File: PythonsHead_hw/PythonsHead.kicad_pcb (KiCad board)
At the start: 2 copper layers, 88.4 x 78.7 mm, 254 parts, among them Q1 IRLML9303, Q10 IRLML9303, Q11 IRLML9303, Q12 IRLML9303, Q13 IRLML6401, Q14 IRLML6244, Q15 IRLML6401, Q16 IRLML6244, Q17 IRLML6401, Q18 IRLML6244, Q19 IRLML6401, Q2 IRLML9303, Q20 IRLML6244, Q21 IRLML6401, Q22 IRLML6244, Q23 IRLML6401, Q24 IRLML6244, Q25 IRLML6401, Q26 IRLML6244, Q27 IRLML6401, Q28 IRLML6244, Q29 IRLML9303, Q3 IRLML9303, Q30 IRLML9303, Q31 IRLML9303, Q32 IRLML9303, Q33 IRLML6401, Q34 IRLML6244, Q35 IRLML6401, Q36 IRLML6244, Q37 IRLML6401, Q38 IRLML6244, Q39 IRLML6401, Q4 IRLML9303, Q40 IRLML6244, Q41 IRLML6401, Q42 IRLML6244, Q43 IRLML6401, Q44 IRLML6244, Q45 IRLML6401, Q46 IRLML6244, Q47 IRLML6401, Q48 IRLML6244, Q49 IRF8313, Q5 IRLML9303, Q6 IRLML9303, Q7 IRLML9303, Q8 IRLML9303, Q9 IRLML9303

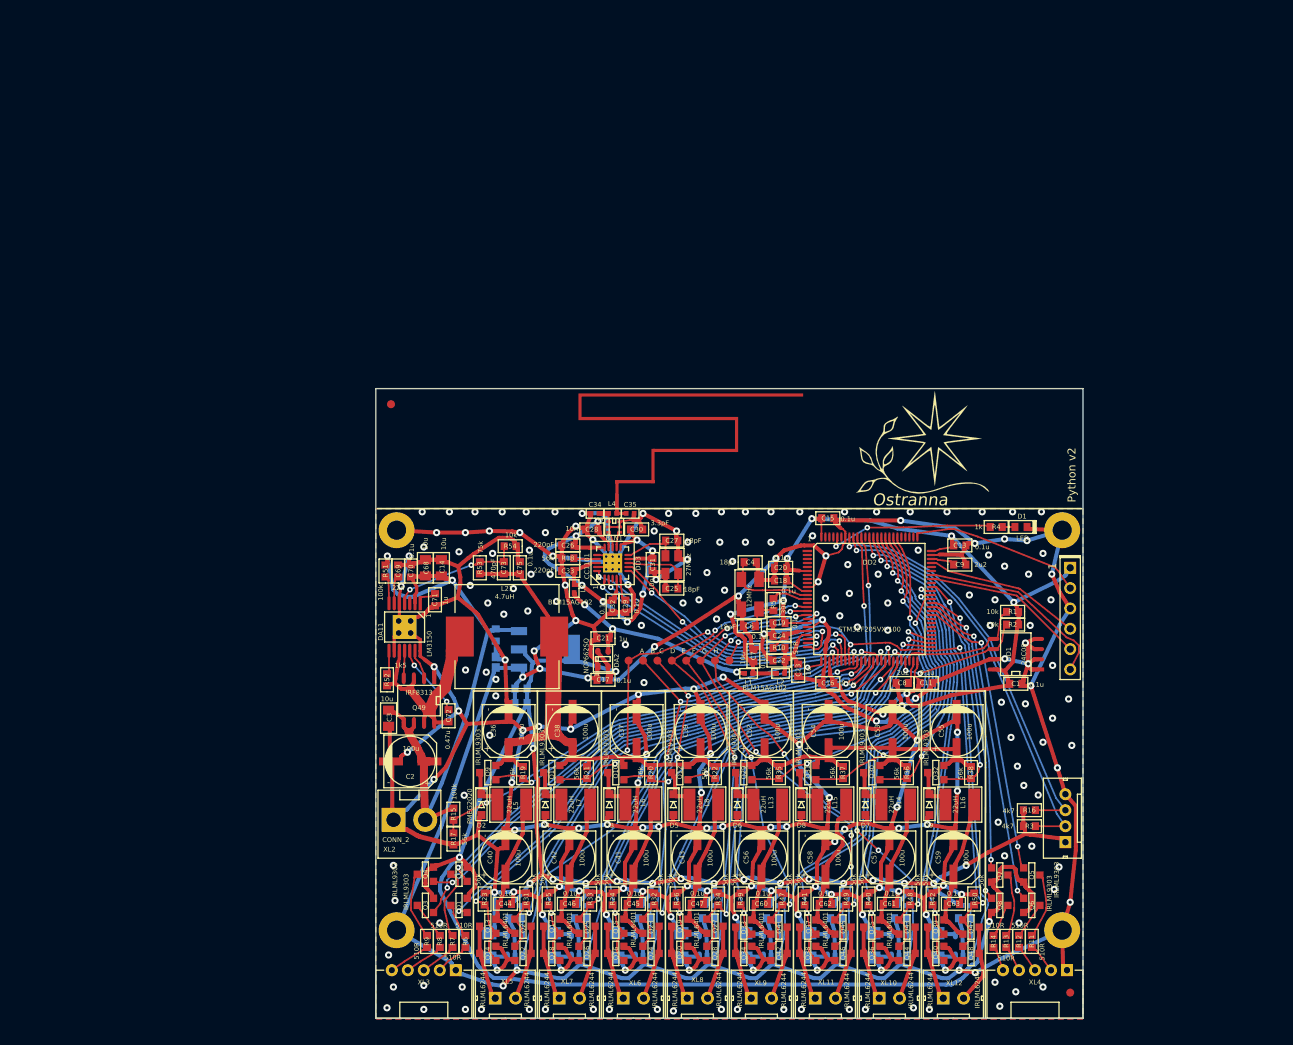
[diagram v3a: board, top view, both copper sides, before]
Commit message: SCH done, proceeding with layout
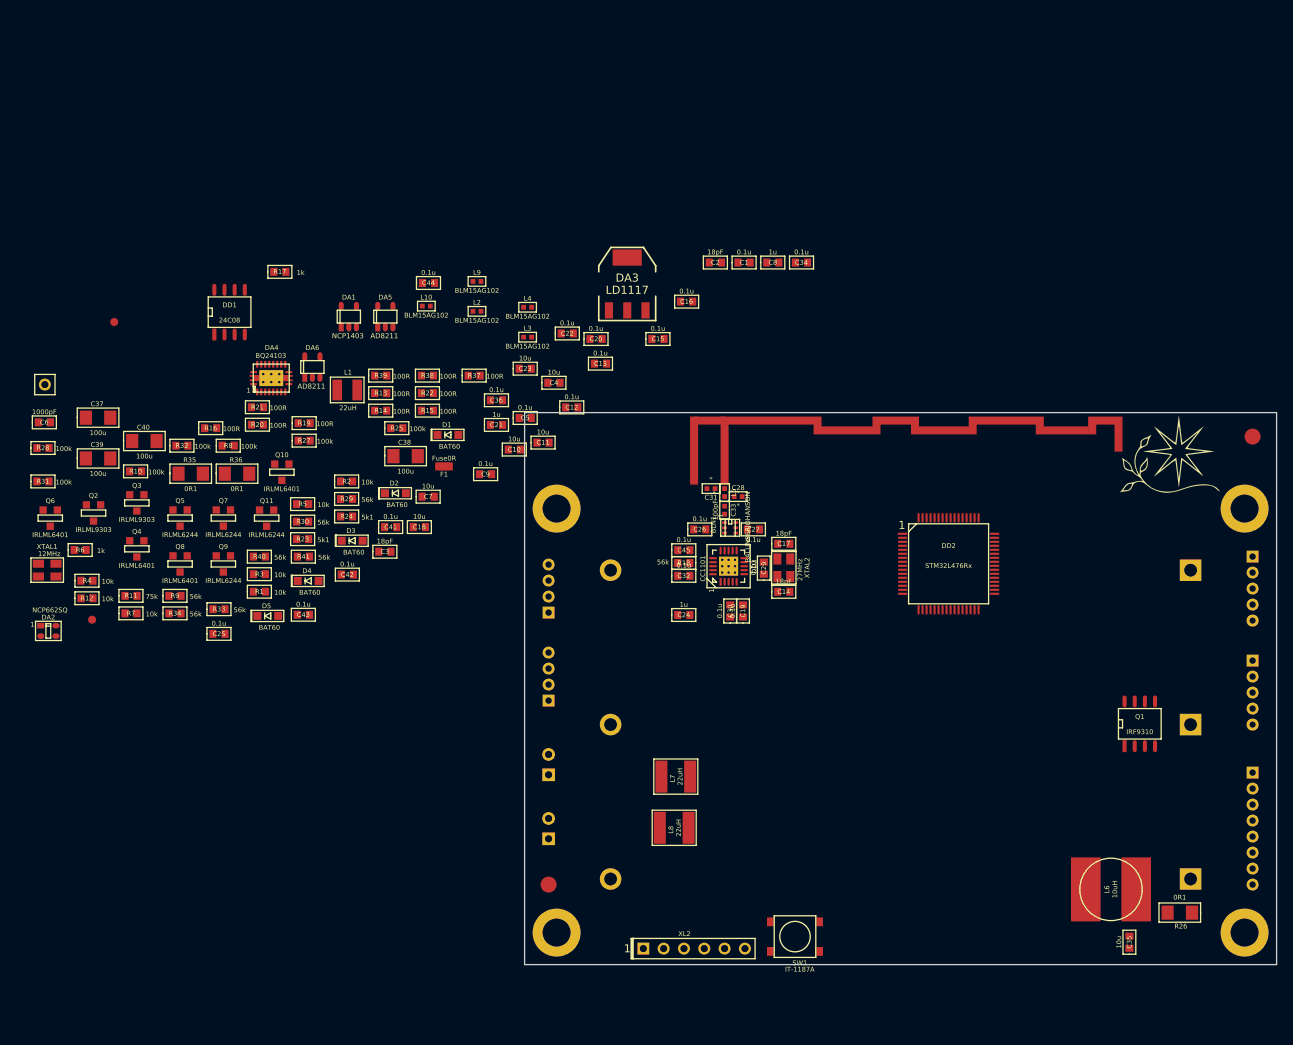
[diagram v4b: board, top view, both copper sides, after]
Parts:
- removed C46, C47, C48, C49, C50, C51, C60, C61, C62, C63, C64, C65, C66, C67, C70, C75: 0.1u, Capacitors:CAP_0603
- removed C52, C53, C54, C55, C56, C57, C58, C59: 100u, Capacitors:SMD_D6d3
- removed C68: 10u, Capacitors:CAP_0805
- removed C69: 22n, Capacitors:CAP_0603
- removed C71: 1u, Capacitors:CAP_0603
- removed C72: 0.47u, Capacitors:CAP_0603
- removed C73: 470pF, Capacitors:CAP_0603
- removed D6, D7, D8, D9: PMEG2020, Diodes:SOD323
- removed DA10, DA7, DA8, DA9: AD8211, SOT:SOT23-5
- removed DA11: LM3150, SO_DIL_TSSOP:HTSSOP14
- removed L11, L12, L17, L18, L19, L20: BLM15AG102, Inductors:IND_0402
- removed L13, L14, L15, L16: 22uH, Inductors:SRN5040
- removed L21: 4.7uH, Inductors:13x13
- removed Q12, Q29, Q30, Q31, Q32: IRLML9303, SOT:SOT23-3
- removed Q13, Q15, Q17, Q19, Q21, Q23, Q25, Q27, Q33, Q35, Q37, Q39, Q41, Q43, Q45, Q47: IRLML6401, SOT:SOT23-3
- removed Q14, Q16, Q18, Q20, Q22, Q24, Q26, Q28, Q34, Q36, Q38, Q40, Q42, Q44, Q46, Q48: IRLML6244, SOT:SOT23-3
- removed Q49: IRF8313, SO_DIL_TSSOP:SO8_150MIL
- removed R42, R47, R48, R49, R50: 56k, Resistors:RES_0603
- removed R43, R44, R45, R46: 0R1, Resistors:RES_1206
- removed R51: 100k, Resistors:RES_0603
- removed R52: 1k5, Resistors:RES_0603
- removed R53: 75k, Resistors:RES_0603
- removed R54: 10k, Resistors:RES_0603
- removed TP3, TP4, TP5, TP6, TP7, TP8: TESTPOINT, PCB:TESTPOINT_1MM
- removed XL10, XL11, XL12: CONN_2, Connectors:W02_Pitch_2d54
- removed XL14: CONN_4, Connectors:WB-04(MW-4M)
- added BAT1: BATx3, Installation:18650x3, B.Cu at (144.0, 108.0)
- added SW1: IT-1187A, BtnsSwitches:BTN_4x4_SMD, F.Cu at (130.8, 134.5)
- ANT1: value ANT_PCB_MONO -> ANT_PCB_MONO_2PIN; footprint Radio:ANT_868_ARMLETG -> Radio:ANT_868_IFA_SIMPLEJOY
- C10: value 0.1u -> 10u; moved to F.Cu
- C11, C18: value 0.1u -> 10u
- C12: value 10u -> 0.1u; moved to F.Cu
- C14, C3: value 10u -> 18pF; footprint Capacitors:CAP_0805 -> Capacitors:CAP_0603
- C17: value 0.1u -> 18pF
- C2: value 100u -> 18pF; footprint Capacitors:SMD_D6d3 -> Capacitors:CAP_0603
- C23: value 1u -> 10u
- C24: value 0.1u -> 1u
- C25, C27: value 18pF -> 0.1u
- C26: value 220pF -> 0.1u
- C28, C31: value 10n -> *; footprint Capacitors:CAP_0603 -> Capacitors:CAP_0402
- C30: value 3.3pF -> 0.1u
- C33: value 220pF -> 100pF; footprint Capacitors:CAP_0603 -> Capacitors:CAP_0402
- C34: value * -> 0.1u; footprint Capacitors:CAP_0402 -> Capacitors:CAP_0603
- C35: value * -> 10u; footprint Capacitors:CAP_0402 -> Capacitors:CAP_0603
- C36, C41, C42, C43: value 100u -> 0.1u; footprint Capacitors:SMD_D6d3 -> Capacitors:CAP_0603
- C37, C38, C39, C40: footprint Capacitors:SMD_D6d3 -> Resistors:RES_1206
- C4: value 18pF -> 10u
- C5, DA5, DA6, L10, L9: moved to F.Cu
- C6: value 18pF -> 1000pF
- C8: value 2u2 -> 1u
- C9: value 2u2 -> 0.1u
- D1: value LED -> BAT60; footprint LEDs:LED_0603 -> Diodes:SOD323
- D2, D3, D4, D5: value PMEG2020 -> BAT60
- DA1: value LD1117 -> NCP1403; footprint SOT:SOT223 -> SOT:SOT23-5; moved to F.Cu
- DA3: value AD8211 -> LD1117; footprint SOT:SOT23-5 -> SOT:SOT223; moved to F.Cu
- DA4: value AD8211 -> BQ24103; footprint SOT:SOT23-5 -> QFN_DFN:RPVQFN-N20; moved to F.Cu
- DD2: value STM32F205VX-100 -> STM32L476Rx; footprint LQFP_TQFP:LQFP100 -> LQFP_TQFP:LQFP64
- F1: footprint Resistors:RES_0603_FUSE -> PCB:FuseShorted; moved to F.Cu
- HOLE1, HOLE2, HOLE3, HOLE4: footprint PCB:Hole2d4_out4d5mm -> PCB:Hole3_5_out6mm
- L1: value BLM15AG102 -> 22uH; footprint Inductors:IND_0402 -> Inductors:IND_1210_LQH32C
- L4: value * -> BLM15AG102
- L5: value 22uH -> *; footprint Inductors:SRN5040 -> Inductors:IND_0402
- L6: value 22uH -> 10uH; footprint Inductors:SRN5040 -> Inductors:SDR0805
- Logo1: footprint Pictures:Ostranna_16d9_13d5 -> Pictures:Ostranna_12d7_10d1
- Q1: value IRLML9303 -> IRF9310; footprint SOT:SOT23-3 -> SO_DIL_TSSOP:SO8_150MIL
- Q10, Q4, Q6, Q8: value IRLML9303 -> IRLML6401
- Q11, Q5, Q7, Q9: value IRLML9303 -> IRLML6244
- R10: value 51R -> 100k
- R11: value 510R -> 75k
- R12, R7: value 510R -> 10k
- R13, R14: value 510R -> 100R
- R15: value 100k -> 100R
- R16: value 4k7 -> 100R
- R17: value 56k -> 1k
- R19, R20, R21, R22, R37, R38, R39: value 56k -> 100R
- R23, R24: value 56k -> 5k1
- R25, R31, R32: value 56k -> 100k
- R26, R35, R36: value 56k -> 0R1; footprint Resistors:RES_0603 -> Resistors:RES_1206
- R27, R28: value 0R1 -> 100k; footprint Resistors:RES_1206 -> Resistors:RES_0603; moved to F.Cu
- R29, R30: value 0R1 -> 56k; footprint Resistors:RES_1206 -> Resistors:RES_0603; moved to F.Cu
- R3: value 4k7 -> 10k
- R4: value 1k -> 10k
- R5: value 390R -> 10k
- R6: value 510R -> 1k
- R8: value 510R -> 100k
- R9: value 510R -> 56k
- RP1, RP2: footprint PCB:REF_POINT_1MM -> PCB:REF_POINT_2MM
- XL1: value CONN_6 -> CONN_4; footprint Connectors:PLS-6 -> Connectors:WB-04(MW-4M); moved to B.Cu
- XL2: value CONN_2 -> CONN_6; footprint Connectors:PWL2-02 -> Connectors:PLS-6
- XL3: value CONN_5 -> CONN_4; footprint Connectors:WB-05R(MW-5MR) -> Connectors:WB-04(MW-4M); moved to B.Cu
- XL4: footprint Connectors:WB-05R(MW-5MR) -> Connectors:WB-05(MW-5M); moved to B.Cu
- XL5: value CONN_2 -> CONN_5; footprint Connectors:W02_Pitch_2d54 -> Connectors:WB-05(MW-5M); moved to B.Cu
- XL6: value CONN_2 -> CONN_1; footprint Connectors:W02_Pitch_2d54 -> Connectors:PLS-1Rnd
- XL7, XL8: moved to B.Cu
- XL9: value CONN_2 -> WB-08; footprint Connectors:W02_Pitch_2d54 -> Connectors:WB-08(MW-8M); moved to B.Cu
- XTAL1: footprint Quartz:0503x4-4 -> Quartz:03225C4
- moved Q6 131.9 mm to (37.7, 82.2), turned to 0 degrees
- moved R12 124.2 mm to (42.3, 92.2), turned to 0 degrees
- moved R11 120.6 mm to (47.8, 91.9), turned to 0 degrees
- moved Q5 115.4 mm to (53.9, 82.2), turned to 0 degrees
- moved R4 113.9 mm to (42.3, 90.0), turned to 0 degrees
- moved R16 112.9 mm to (57.8, 70.9)
- moved Q8 111.0 mm to (53.9, 87.9), turned to 0 degrees
- moved DD1 107.2 mm to (60.1, 56.4), turned to 0 degrees
- moved Q7 106.8 mm to (59.3, 82.2), turned to 0 degrees
- moved XL6 106.3 mm to (37.0, 65.5)
- moved HOLE4 106.0 mm to (187.0, 81.0)
- moved HOLE3 106.0 mm to (187.0, 134.0)
- moved R13 104.0 mm to (79.0, 66.6), turned to 0 degrees
- moved R14 101.3 mm to (79.0, 68.8), turned to 0 degrees
- moved R3 101.3 mm to (63.8, 89.2)
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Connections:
- BLN1 pad 1: /ANT1 -> Net-(BLN1-Pad1)
- C10 pad 1: GND -> GNDPWR
- C10 pad 2: +5V -> /PWR_MID
- C11 pad 1: GND -> GNDPWR
- C11 pad 2: PwrMCU -> /PWR_MID
- C12 pad 2: +5V -> PwrMCU
- C14 pad 1: +BATT -> Net-(C14-Pad1)
- C14 pad 2: GNDPWR -> GND
- C17 pad 1: +5V -> Net-(C17-Pad1)
- C18 pad 1: GND -> GNDPWR
- C18 pad 2: PwrMCU -> +5V
- C19 pad 2: PwrMCU -> Net-(C19-Pad2)
- C2 pad 1: +BATT -> Net-(C2-Pad1)
- C2 pad 2: GNDPWR -> GND
- C20 pad 2: PwrMCU -> /VDDA
- C21 pad 1: +3.3V -> GND
- C21 pad 2: GND -> /VDDA
- C22 pad 1: GND -> Net-(C22-Pad1)
- C22 pad 2: /VDDA -> GNDPWR
- C23 pad 1: GND -> GNDPWR
- C23 pad 2: /VDDA -> /5V_USB
- C24 pad 2: /Vref+ -> VCC
- C25 pad 1: Net-(C25-Pad1) -> /5V_USB
- C25 pad 2: GND -> GNDPWR
- C27 pad 1: Net-(C27-Pad1) -> GND
- C27 pad 2: GND -> VCC
- C28 pad 1: GND -> /ANT1
- C28 pad 2: VCC -> GND
- C29 pad 2: Net-(C29-Pad2) -> VCC
- C3 pad 1: +BATT -> Net-(C3-Pad1)
- C3 pad 2: GNDPWR -> GND
- C31 pad 1: GND -> /ANT2
- C31 pad 2: VCC -> GND
- C33 pad 1: GND -> /ANT1
- C33 pad 2: VCC -> Net-(BLN1-Pad1)
- C34 pad 1: /ANT1 -> /VTSB
- C34 pad 2: GND -> GNDPWR
- C35 pad 1: /ANT2 -> GNDPWR
- C35 pad 2: GND -> Net-(C35-Pad2)
- C36 pad 1: VAA -> Net-(C35-Pad2)
- C37 pad 1: VAA -> +BATT
- C38 pad 1: VAA -> +BATT
- C39 pad 1: VAA -> /HTRA_PWR
- C4 pad 1: Net-(C4-Pad1) -> GNDPWR
- C4 pad 2: GND -> +BATT
- C40 pad 1: /HTRA_PWR -> /HTRB_PWR
- C41 pad 1: /HTRC_PWR -> GNDPWR
- C41 pad 2: GNDPWR -> /HTRA_PWR
- C42 pad 1: /HTRB_PWR -> GNDPWR
- C42 pad 2: GNDPWR -> /HTRB_PWR
- C43 pad 1: /HTRD_PWR -> GND
- C43 pad 2: GNDPWR -> Net-(C43-Pad2)
- C44 pad 1: GNDPWR -> GND
- C44 pad 2: /HTRA_PWR -> Net-(C44-Pad2)
- C45 pad 1: GNDPWR -> GND
- C45 pad 2: /HTRC_PWR -> VCC
- C5 pad 1: GNDPWR -> Net-(C5-Pad1)
- C5 pad 2: +BATT -> GND
- C6 pad 2: GND -> /PWR_MID
- C8 pad 1: Net-(C8-Pad1) -> +3.3V
- C9 pad 1: Net-(C9-Pad1) -> GND
- C9 pad 2: GND -> PwrMCU
- D1 pad A: Net-(D1-PadA) -> /5V_USB
- D1 pad C: GND -> Net-(C5-Pad1)
- D2 pad A: GNDPWR -> +BATT
- D2 pad C: Net-(D2-PadC) -> Net-(C5-Pad1)
- D3 pad A: GNDPWR -> /PWR_LX
- D3 pad C: Net-(D3-PadC) -> /PWR_MID
- DA1 pad 1: GND -> /5V_EN
- DA1 pad 2: +5V -> Net-(C6-Pad1)
- DA2 pad 2: +5V -> Net-(C5-Pad1)
- DA2 pad 4: +5V -> Net-(C5-Pad1)
- DA3 pad 1: /HTRA_CURR -> GNDPWR
- DA3 pad 2: GND -> +5V
- DA3 pad 3: /HTRA_GND -> /PWR_MID
- DA4 pad 1: /HTRC_CURR -> Net-(DA4-Pad1)
- DA4 pad 2: GND -> /STAT1
- DA4 pad 3: /HTRC_GND -> /5V_USB
- DA4 pad 4: GNDPWR -> /5V_USB
- DA4 pad 5: Net-(C49-Pad2) -> (no net)
- DA5 pad 1: /HTRB_CURR -> /HTRA_CURR
- DA5 pad 3: /HTRB_GND -> /HTRA_GND
- DA5 pad 5: Net-(C50-Pad2) -> Net-(C43-Pad2)
- DA6 pad 1: /HTRD_CURR -> /HTRB_CURR
- DA6 pad 3: /HTRD_GND -> /HTRB_GND
- DA6 pad 5: Net-(C51-Pad2) -> Net-(C44-Pad2)
- DD2 pad 1: (no net) -> PwrMCU
- DD2 pad 10: GND -> /HTRA_DIR1
- DD2 pad 11: PwrMCU -> /HTRA_DIR2
- DD2 pad 12: Net-(C4-Pad1) -> GND
- DD2 pad 13: Net-(DD2-Pad13) -> /VDDA
- DD2 pad 14: (no net) -> /CC_GDO0
- DD2 pad 15: /HTRD_CURR -> /CC_CS
- DD2 pad 16: /HTRE_CURR -> /HTRA_CURR
- DD2 pad 17: /HTRF_CURR -> /HTRB_CURR
- DD2 pad 18: /HTRG_CURR -> GND
- DD2 pad 20: GND -> /BAT_MEAS
- DD2 pad 21: /Vref+ -> /CC_SCK
- DD2 pad 22: /VDDA -> /CC_MISO
- DD2 pad 23: /CC_GDO0 -> /CC_MOSI
- DD2 pad 24: /CC_CS -> /HTRB_DIR1
- DD2 pad 25: /HTRA_CURR -> /HTRB_DIR2
- DD2 pad 26: /HTRB_CURR -> /LED7_PWM_CTRL
- DD2 pad 27: GND -> /LED8_PWM_CTRL
- DD2 pad 28: PwrMCU -> (no net)
- DD2 pad 29: /HTRC_CURR -> /SCL_SNS2
- DD2 pad 30: /CC_SCK -> /SDA_SNS2
- DD2 pad 31: /CC_MISO -> GND
- DD2 pad 32: /CC_MOSI -> PwrMCU
- DD2 pad 33: /HTRH_CURR -> (no net)
- DD2 pad 34: /BAT_MEAS -> (no net)
- DD2 pad 35: /LED3_PWM_CTRL -> /HTRA_PWM_CTRL
- DD2 pad 36: /LED4_PWM_CTRL -> /HTRB_PWM_CTRL
- DD2 pad 37: (no net) -> /LED1_PWM_CTRL
- DD2 pad 38: /HTRA_DIR1 -> /LED2_PWM_CTRL
- DD2 pad 39: /HTRA_DIR2 -> /LED3_PWM_CTRL
- DD2 pad 40: /HTRA_PWM_CTRL -> /LED4_PWM_CTRL
- DD2 pad 41: /HTRB_DIR1 -> Net-(DD2-Pad41)
- DD2 pad 42: /HTRB_PWM_CTRL -> /UART_TX
- DD2 pad 43: /HTRB_DIR2 -> /UART_RX
- DD2 pad 44: /HTRC_PWM_CTRL -> /D-
- DD2 pad 45: /HTRD_PWM_CTRL -> /D+
- DD2 pad 46: /HTRC_DIR1 -> /SWDIO
- DD2 pad 47: /SCL_EE -> GND
- DD2 pad 48: /SDA_EE -> PwrMCU
- DD2 pad 49: Net-(C8-Pad1) -> /SWCLK
- DD2 pad 5: (no net) -> Net-(C2-Pad1)
- DD2 pad 50: PwrMCU -> /5V_EN
- DD2 pad 51: /HTRC_DIR2 -> /STAT1
- DD2 pad 52: /HTRD_DIR1 -> /STAT2
- DD2 pad 53: /HTRD_DIR2 -> /CHARGE_EN
- DD2 pad 55: (no net) -> /R
- DD2 pad 56: (no net) -> /LED5_PWM_CTRL
- DD2 pad 57: (no net) -> /LED6_PWM_CTRL
- DD2 pad 58: (no net) -> /G
- DD2 pad 59: /LED5_PWM_CTRL -> /B
- DD2 pad 6: PwrMCU -> Net-(DD2-Pad6)
- DD2 pad 60: /LED6_PWM_CTRL -> Net-(DD2-Pad60)
- DD2 pad 61: /LED7_PWM_CTRL -> /SCL_SNS1
- DD2 pad 62: /LED8_PWM_CTRL -> /SDA_SNS1
- DD2 pad 63: /HTRE_PWM_CTRL -> GND
- DD2 pad 64: /HTRF_PWM_CTRL -> PwrMCU
- DD2 pad 8: (no net) -> /SCL_EE
- DD2 pad 9: (no net) -> /SDA_EE
- DD3 pad 10: Net-(C27-Pad1) -> Net-(C17-Pad1)
- DD3 pad 5: Net-(C29-Pad2) -> Net-(C19-Pad2)
- DD3 pad 8: Net-(C25-Pad1) -> Net-(C14-Pad1)
- L1 pad 1: PwrMCU -> /PWR_LX
- L1 pad 2: +3.3V -> +BATT
- L10 pad 2: Net-(C49-Pad2) -> Net-(C44-Pad2)
- L2 pad 1: /VDDA -> PwrMCU
- L2 pad 2: PwrMCU -> +3.3V
- L3 pad 1: VCC -> /VDDA
- L3 pad 2: +3.3V -> PwrMCU
- L4 pad 1: /ANT2 -> VCC
- L4 pad 2: /ANT1 -> +3.3V
- L5 pad 1: /HTRA_PWR -> /ANT2
- L5 pad 2: Net-(D2-PadC) -> /ANT1
- L6 pad 1: /HTRC_PWR -> Net-(C35-Pad2)
- L6 pad 2: Net-(D3-PadC) -> Net-(DA4-Pad1)
- L7 pad 1: /HTRB_PWR -> /HTRA_PWR
- L8 pad 1: /HTRD_PWR -> /HTRB_PWR
- L9 pad 2: Net-(C48-Pad2) -> Net-(C43-Pad2)
- Q1 pad 1: /LED1_PWM_CTRL -> /BATTERY
- Q1 pad 2: +5V -> /BATTERY
- Q1 pad 3: Net-(Q1-Pad3) -> /BATTERY
- Q10 pad 1: /HTRC_PWM_CTRL -> /HTRB_DIR2
- Q10 pad 2: VAA -> /HTRB_PWR
- Q10 pad 3: Net-(D3-PadC) -> /HTRB2
- Q11 pad 1: /HTRB_PWM_CTRL -> /HTRB_DIR2
- Q11 pad 2: VAA -> /HTRB_GND
- Q11 pad 3: Net-(D4-PadC) -> /HTRB2
- Q2 pad 1: /LED2_PWM_CTRL -> /HTRA_PWM_CTRL
- Q2 pad 2: +5V -> +BATT
- Q2 pad 3: Net-(Q2-Pad3) -> Net-(D4-PadC)
- Q3 pad 1: /LED3_PWM_CTRL -> /HTRB_PWM_CTRL
- Q3 pad 2: +5V -> +BATT
- Q3 pad 3: Net-(Q3-Pad3) -> Net-(D5-PadC)
- Q4 pad 1: /LED4_PWM_CTRL -> /HTRA_DIR1
- Q4 pad 2: +5V -> /HTRA_PWR
- Q4 pad 3: Net-(Q4-Pad3) -> /HTRA1
- Q5 pad 1: /LED5_PWM_CTRL -> /HTRA_DIR1
- Q5 pad 2: +5V -> /HTRA_GND
- Q5 pad 3: Net-(Q5-Pad3) -> /HTRA1
- Q6 pad 1: /LED6_PWM_CTRL -> /HTRB_DIR1
- Q6 pad 2: +5V -> /HTRB_PWR
- Q6 pad 3: Net-(Q6-Pad3) -> /HTRB1
- Q7 pad 1: /LED7_PWM_CTRL -> /HTRB_DIR1
- Q7 pad 2: +5V -> /HTRB_GND
- Q7 pad 3: Net-(Q7-Pad3) -> /HTRB1
- Q8 pad 1: /LED8_PWM_CTRL -> /HTRA_DIR2
- Q8 pad 2: +5V -> /HTRA_PWR
- Q8 pad 3: Net-(Q8-Pad3) -> /HTRA2
- Q9 pad 1: /HTRA_PWM_CTRL -> /HTRA_DIR2
- Q9 pad 2: VAA -> /HTRA_GND
- Q9 pad 3: Net-(D2-PadC) -> /HTRA2
- R1 pad 1: PwrMCU -> +5V
- R1 pad 2: /SDA_EE -> /SDA_SNS1
- R10 pad 1: /Vref+ -> GNDPWR
- R10 pad 2: /VDDA -> /5V_EN
- R11 pad 1: Net-(R11-Pad1) -> Net-(C6-Pad1)
- R11 pad 2: Net-(Q5-Pad3) -> /PWR_MID
- R12 pad 1: Net-(R12-Pad1) -> GNDPWR
- R12 pad 2: Net-(Q6-Pad3) -> Net-(C6-Pad1)
- R13 pad 2: Net-(Q7-Pad3) -> /LED1_PWM_CTRL
- R14 pad 2: Net-(Q8-Pad3) -> /LED2_PWM_CTRL
- R15 pad 1: +BATT -> Net-(R15-Pad1)
- R15 pad 2: /BAT_MEAS -> /LED3_PWM_CTRL
- R16 pad 1: +5V -> Net-(R16-Pad1)
- R16 pad 2: /SDA_SNS -> /LED4_PWM_CTRL
- R17 pad 1: /BAT_MEAS -> Net-(DD2-Pad41)
- R17 pad 2: GNDPWR -> /5V_USB
- R19 pad 1: VAA -> Net-(R19-Pad1)
- R19 pad 2: /HTRA_PWM_CTRL -> /LED5_PWM_CTRL
- R2 pad 1: /SCL_EE -> PwrMCU
- R2 pad 2: PwrMCU -> /SDA_EE
- R20 pad 1: VAA -> Net-(R20-Pad1)
- R20 pad 2: /HTRC_PWM_CTRL -> /LED6_PWM_CTRL
- R21 pad 1: VAA -> Net-(R21-Pad1)
- R21 pad 2: /HTRB_PWM_CTRL -> /LED7_PWM_CTRL
- R22 pad 1: VAA -> Net-(R22-Pad1)
- R22 pad 2: /HTRD_PWM_CTRL -> /LED8_PWM_CTRL
- R23 pad 1: /HTRA_DIR1 -> GNDPWR
- R23 pad 2: GNDPWR -> Net-(DA4-Pad8)
- R24 pad 1: /HTRC_DIR1 -> GNDPWR
- R24 pad 2: GNDPWR -> Net-(DA4-Pad9)
- R25 pad 1: /HTRB_DIR1 -> Net-(DA4-Pad12)
- R26 pad 1: /HTRD_DIR1 -> /BATTERY
- R26 pad 2: GNDPWR -> Net-(C35-Pad2)
- R27 pad 1: /HTRA_GND -> /VTSB
- R27 pad 2: GNDPWR -> Net-(DA4-Pad12)
- R28 pad 1: /HTRC_GND -> /BATTERY
- R28 pad 2: GNDPWR -> /CHARGE_EN
- R29 pad 1: /HTRB_GND -> +BATT
- R29 pad 2: GNDPWR -> /HTRA_PWM_CTRL
- R3 pad 1: +5V -> /SCL_EE
- R3 pad 2: /SCL_SNS -> PwrMCU
- R30 pad 1: /HTRD_GND -> +BATT
- R30 pad 2: GNDPWR -> /HTRB_PWM_CTRL
- R31 pad 1: /HTRA_DIR2 -> +BATT
- R31 pad 2: GNDPWR -> /BAT_MEAS
- R32 pad 1: /HTRC_DIR2 -> /BAT_MEAS
- R33 pad 1: /HTRB_DIR2 -> /HTRA_DIR1
- R34 pad 1: /HTRD_DIR2 -> /HTRB_DIR1
- R35 pad 1: VAA -> /HTRA_GND
- R35 pad 2: /HTRE_PWM_CTRL -> GNDPWR
- R36 pad 1: VAA -> /HTRB_GND
- R36 pad 2: /HTRG_PWM_CTRL -> GNDPWR
- R37 pad 1: VAA -> Net-(R37-Pad1)
- R37 pad 2: /HTRF_PWM_CTRL -> /R
- R38 pad 1: VAA -> Net-(R38-Pad1)
- R38 pad 2: /HTRH_PWM_CTRL -> /G
- R39 pad 1: /HTRE_DIR1 -> Net-(R39-Pad1)
- R39 pad 2: GNDPWR -> /B
- R4 pad 1: Net-(D1-PadA) -> +5V
- R4 pad 2: /LED -> /SCL_SNS1
- R40 pad 1: /HTRG_DIR1 -> /HTRA_DIR2
- R41 pad 1: /HTRF_DIR1 -> /HTRB_DIR2
- R5 pad 1: Net-(DD2-Pad13) -> +5V
- R5 pad 2: Net-(C6-Pad1) -> /SDA_SNS2
- R6 pad 1: Net-(R6-Pad1) -> Net-(C3-Pad1)
- R6 pad 2: Net-(Q1-Pad3) -> Net-(DD2-Pad6)
- R7 pad 1: Net-(R7-Pad1) -> +5V
- R7 pad 2: Net-(Q2-Pad3) -> /SCL_SNS2
- R8 pad 1: Net-(R8-Pad1) -> /OnOff
- R8 pad 2: Net-(Q3-Pad3) -> /BATTERY
- R9 pad 1: Net-(R9-Pad1) -> Net-(DD2-Pad60)
- R9 pad 2: Net-(Q4-Pad3) -> GND
- TP2 pad 1: /HTRC_CURR -> /HTRB_CURR
- XL1 pad 1: PwrMCU -> +5V
- XL1 pad 2: /SWCLK -> /SCL_SNS1
- XL1 pad 3: GND -> /SDA_SNS1
- XL1 pad 4: /SWDIO -> GND
- XL2 pad 1: GNDPWR -> +3.3V
- XL2 pad 2: +BATT -> /SWCLK
- XL3 pad 1: GND -> +5V
- XL3 pad 2: Net-(R6-Pad1) -> /SCL_SNS2
- XL3 pad 3: Net-(R7-Pad1) -> /SDA_SNS2
- XL3 pad 4: Net-(R8-Pad1) -> GND
- XL4 pad 2: Net-(R11-Pad1) -> Net-(R13-Pad1)
- XL4 pad 3: Net-(R12-Pad1) -> Net-(R14-Pad1)
- XL4 pad 4: Net-(R13-Pad1) -> Net-(R15-Pad1)
- XL4 pad 5: Net-(R14-Pad1) -> Net-(R16-Pad1)
- XL5 pad 1: /HTRA1 -> GND
- XL5 pad 2: /HTRA2 -> Net-(R19-Pad1)
- XL6 pad 1: /HTRC1 -> GND
- XL7 pad 1: /HTRB1 -> /HTRA1
- XL7 pad 2: /HTRB2 -> /HTRA2
- XL8 pad 1: /HTRD1 -> /HTRB1
- XL8 pad 2: /HTRD2 -> /HTRB2
- XL9 pad 1: /HTRE1 -> /5V_USB
- XL9 pad 2: /HTRE2 -> /D-
- XTAL1 pad 1: Net-(C4-Pad1) -> Net-(C2-Pad1)
- XTAL1 pad 2: Net-(C6-Pad1) -> Net-(C3-Pad1)
- XTAL2 pad 1: Net-(C25-Pad1) -> Net-(C14-Pad1)
- XTAL2 pad 2: Net-(C27-Pad1) -> Net-(C17-Pad1)
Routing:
- net GNDPWR: track 574.9 -> 0.00 mm, vias 61 -> 0
- net GND: track 560.4 -> 0.00 mm, vias 44 -> 0
- net +5V: track 286.6 -> 0.00 mm, vias 19 -> 0
- net PwrMCU: track 137.3 -> 0.00 mm, vias 8 -> 0
- net VAA: track 125.9 -> 0.00 mm
- net +BATT: track 83.8 -> 0.00 mm, vias 2 -> 0
- net /LED1_PWM_CTRL: track 79.8 -> 0.00 mm, vias 2 -> 0
- net /LED2_PWM_CTRL: track 76.2 -> 0.00 mm, vias 2 -> 0
- net /HTRH_CURR: track 73.6 -> 0.00 mm, vias 3 -> 0
- net /HTRE_DIR1: track 73.4 -> 0.00 mm, vias 2 -> 0
- net /HTRA_CURR: track 70.4 -> 0.00 mm, vias 3 -> 0
- net /HTRA_DIR1: track 69.9 -> 0.00 mm, vias 2 -> 0
- net /HTRB_DIR1: track 67.8 -> 0.00 mm, vias 2 -> 0
- net /HTRA_DIR2: track 66.0 -> 0.00 mm, vias 2 -> 0
- net /HTRF_DIR1: track 65.5 -> 0.00 mm, vias 2 -> 0
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- removed copper zone on B.Cu, net GND
- removed copper zone on F.Cu, net GND
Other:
- board size 88.4 x 78.7 mm -> 94 x 69 mm
- board text removed: "A B C D E F G H"
- board text removed: "Ostranna"
- board text removed: "Python v2"

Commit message: First version of layout
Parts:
- moved R31 140.7 mm to (173.9, 109.2), turned to 90 degrees
- moved R28 138.4 mm to (161.4, 133.7), turned to 90 degrees
- moved R17 134.3 mm to (185.2, 114.0)
- moved R16 129.6 mm to (185.1, 95.0), turned to 180 degrees
- moved R21 127.2 mm to (185.1, 106.0), turned to 180 degrees
- moved R20 126.0 mm to (185.1, 104.0), turned to 180 degrees
- moved R39 123.8 mm to (185.2, 128.0), turned to 180 degrees
- moved R32 123.5 mm to (172.3, 109.2), turned to 270 degrees
- moved R8 121.7 mm to (176.2, 109.2), turned to 90 degrees
- moved R19 119.9 mm to (185.1, 102.0), turned to 180 degrees
- moved R38 117.8 mm to (185.2, 126.0), turned to 180 degrees
- moved DD1 117.0 mm to (170.2, 96.2)
- moved DA4 115.2 mm to (161.1, 128.7), turned to 180 degrees
- moved DA2 113.0 mm to (150.2, 104.5), turned to 180 degrees
- moved R37 111.7 mm to (185.2, 124.0), turned to 180 degrees
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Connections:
- C18 pad 1: GNDPWR -> GND
- DA4 pad PAD: (no net) -> GNDPWR
- HOLE1 pad H: GND -> (no net)
- HOLE2 pad H: GND -> (no net)
- HOLE3 pad H: GND -> (no net)
- HOLE4 pad H: GND -> (no net)
- XL2 pad 1: +3.3V -> PwrMCU

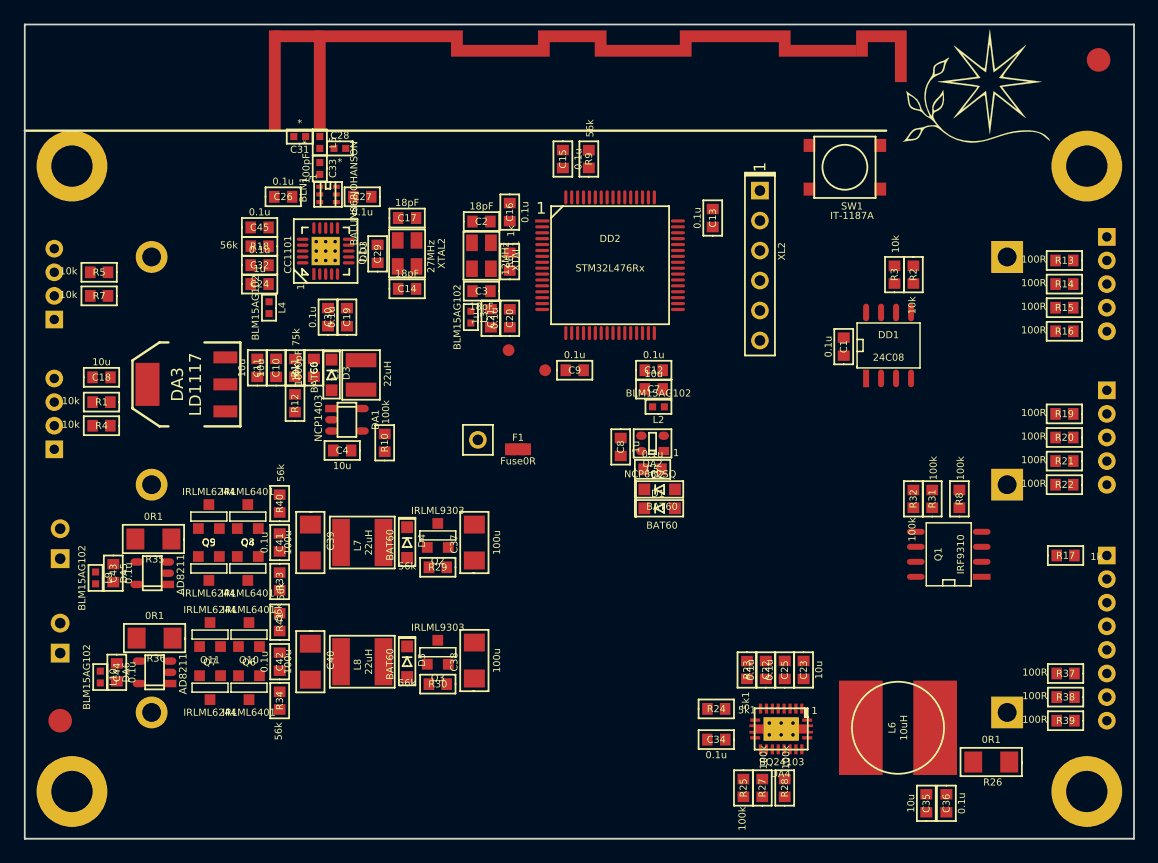
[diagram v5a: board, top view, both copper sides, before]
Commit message: V3 sent to factory
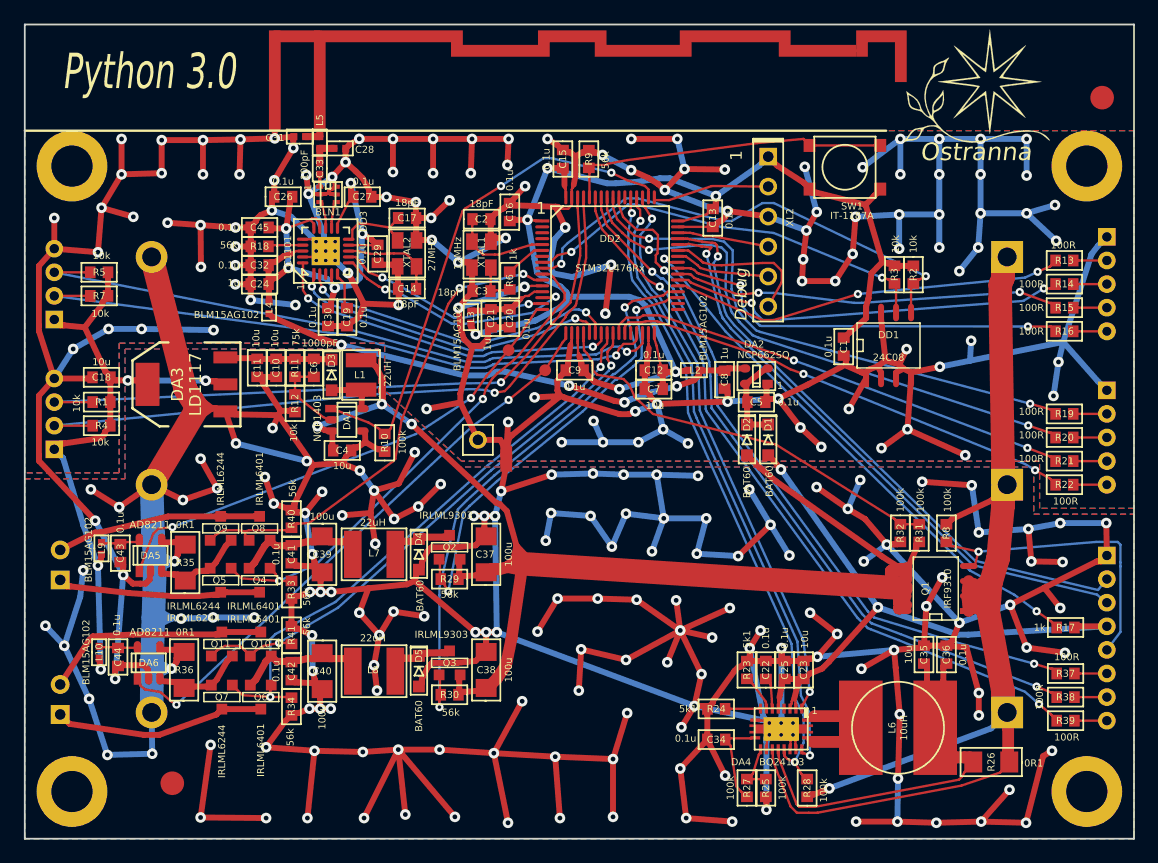
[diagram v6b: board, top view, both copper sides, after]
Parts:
- moved C35 12.6 mm to (173.2, 122.4), turned to 270 degrees
- moved C36 12.6 mm to (175.1, 122.4), turned to 90 degrees
- moved RP2 10.9 mm to (109.5, 133.3)
- moved D1 10.9 mm to (160.0, 104.2), turned to 270 degrees
- moved C5 10.5 mm to (159.0, 101.0)
- moved C8 10.5 mm to (156.3, 99.1)
- moved DA2 10.5 mm to (159.0, 98.8)
- moved D2 8.51 mm to (158.2, 104.2), turned to 270 degrees
- moved R17 6.10 mm to (185.2, 120.1)
- moved XL8 5.20 mm to (100.0, 126.2)
- moved L2 4.31 mm to (153.7, 98.3), turned to 0 degrees
- moved R36 3.68 mm to (110.5, 123.7), turned to 90 degrees
- moved R35 3.36 mm to (110.6, 114.6), turned to 90 degrees
- moved RP1 3.21 mm to (188.3, 75.2)
- moved Q1 3.10 mm to (174.2, 116.8)
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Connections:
- XL9 pad 1: /5V_USB -> GNDPWR
- XL9 pad 2: /D- -> /D+
- XL9 pad 3: /D+ -> /D-
- XL9 pad 4: GNDPWR -> /5V_USB
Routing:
- net GNDPWR: track 0.00 -> 717.4 mm, vias 0 -> 150
- net GND: track 0.00 -> 569.1 mm, vias 0 -> 120
- net +BATT: track 0.00 -> 128.9 mm, vias 0 -> 3
- net PwrMCU: track 0.00 -> 113.6 mm, vias 0 -> 6
- net /BATTERY: track 0.00 -> 105.1 mm, vias 0 -> 1
- net /B: track 0.00 -> 62.3 mm, vias 0 -> 2
- net /G: track 0.00 -> 60.8 mm, vias 0 -> 2
- net /SCL_SNS1: track 0.00 -> 60.3 mm, vias 0 -> 1
- net /R: track 0.00 -> 59.9 mm, vias 0 -> 2
- net /SDA_SNS1: track 0.00 -> 59.1 mm, vias 0 -> 1
- net /5V_USB: track 0.00 -> 56.5 mm, vias 0 -> 2
- net +5V: track 0.00 -> 55.6 mm, vias 0 -> 4
- net /SDA_SNS2: track 0.00 -> 55.2 mm, vias 0 -> 1
- net /CHARGE_EN: track 0.00 -> 54.9 mm, vias 0 -> 2
- net /SCL_SNS2: track 0.00 -> 54.4 mm, vias 0 -> 1
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- added copper zone on B.Cu, net GND
- added copper zone on F.Cu, net GND
- added copper zone on B.Cu, net GNDPWR
- added copper zone on F.Cu, net GNDPWR
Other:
- net class Default: clearance 0.22 -> 0.2; trace_width 0.22 -> 0.2
- net class Wide: clearance 0.22 -> 0.2
- rule trace_clearance: 0.22 -> 0.2
- board text added: "Charge & Switch"
- board text added: "Debug"
- board text added: "LEDs 1"
- board text added: "LEDs 2"
- board text added: "ModA"
- board text added: "ModB"
- board text added: "Ostranna"
- board text added: "Python 3.0"
- board text added: "Sensor1"
- board text added: "Sensor2"
